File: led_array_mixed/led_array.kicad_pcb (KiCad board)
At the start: 2 copper layers, 32 x 32 mm, 66 parts, among them P1 CONN_8, P2 CONN_8

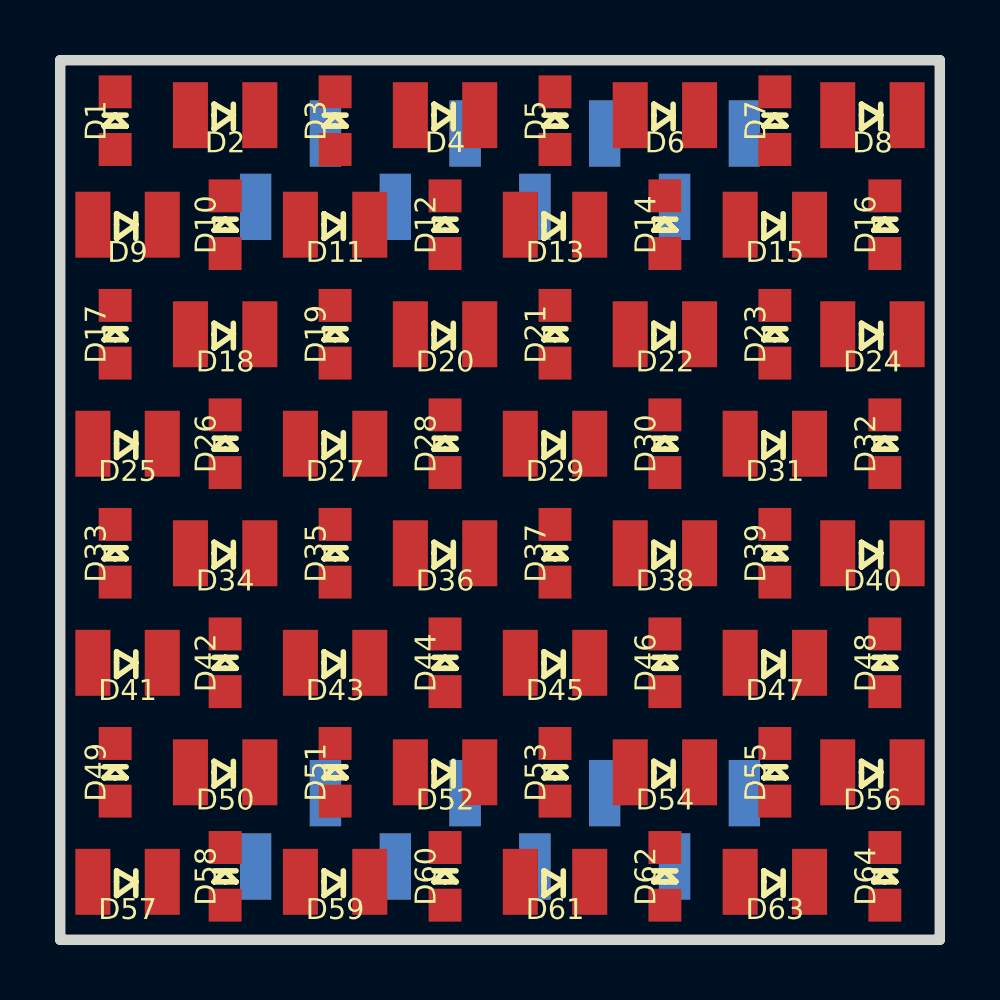
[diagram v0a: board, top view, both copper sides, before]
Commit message: Routed new mixed UV/Green LED array.
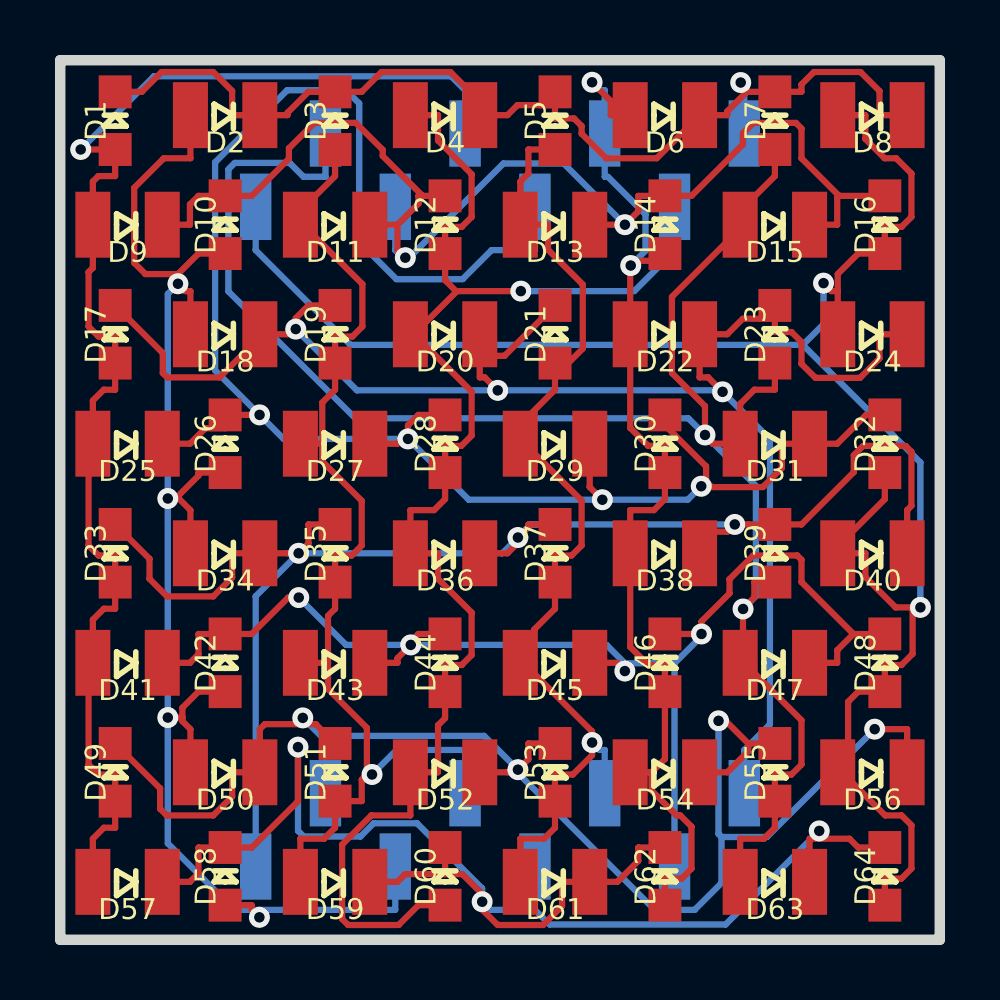
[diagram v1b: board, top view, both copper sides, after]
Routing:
- net /16: track 0.00 -> 72.3 mm, vias 0 -> 2
- net /15: track 0.00 -> 69.5 mm, vias 0 -> 2
- net /12: track 0.00 -> 69.4 mm, vias 0 -> 4
- net /8: track 0.00 -> 62.7 mm, vias 0 -> 3
- net /2: track 0.00 -> 57.7 mm, vias 0 -> 4
- net /1: track 0.00 -> 57.2 mm, vias 0 -> 3
- net /3: track 0.00 -> 55.8 mm, vias 0 -> 4
- net /5: track 0.00 -> 55.4 mm, vias 0 -> 3
- net /10: track 0.00 -> 54.7 mm, vias 0 -> 1
- net /13: track 0.00 -> 51.2 mm, vias 0 -> 1
- net /7: track 0.00 -> 48.7 mm, vias 0 -> 4
- net /14: track 0.00 -> 46.6 mm, vias 0 -> 2
- net /4: track 0.00 -> 40.6 mm, vias 0 -> 1
- net /11: track 0.00 -> 40.1 mm, vias 0 -> 2
- net /9: track 0.00 -> 39.1 mm, vias 0 -> 1
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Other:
- board text added: "Mixed UV/Green 8x8 LED Array V0.1 www.iorodeo.com"
